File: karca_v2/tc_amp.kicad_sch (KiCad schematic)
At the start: 16 parts, among them U17 TLV9304xD, U22 AD8495, U27 TLVH431

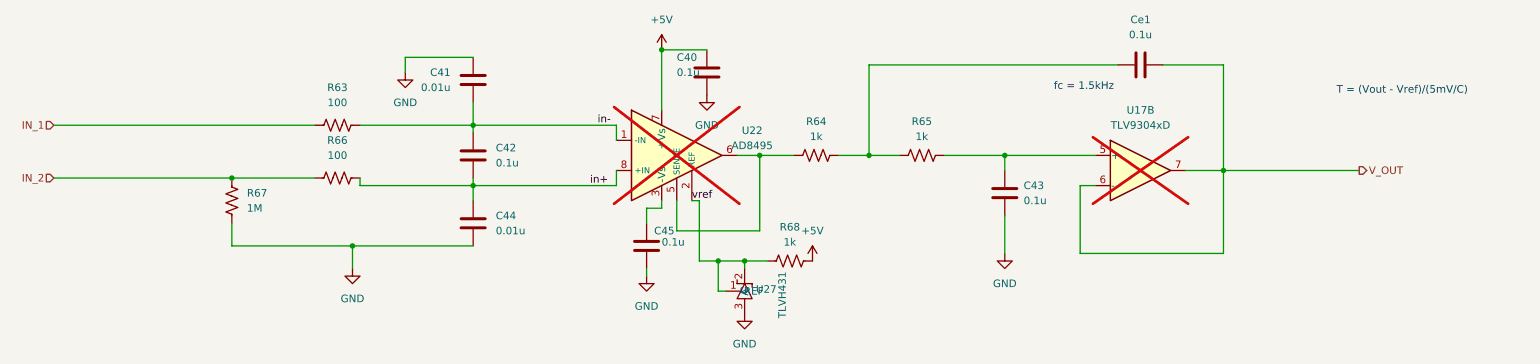
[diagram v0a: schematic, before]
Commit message: new design: chip on board
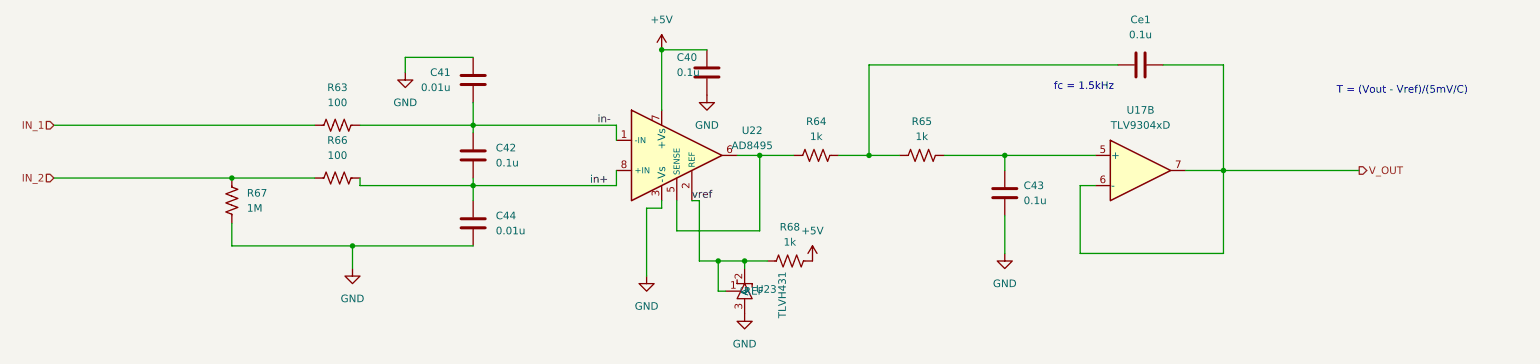
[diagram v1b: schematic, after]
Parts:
- removed C45: 0.1u, Capacitor_SMD:C_1206_3216Metric, symbol Device:C
- U17, U22: now fitted
- renumbered U27 to U23
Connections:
- net GND: now also U22.3 (-Vs)
